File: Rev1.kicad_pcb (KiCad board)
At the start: 2 copper layers, 217.8 x 97.2 mm, 136 parts, among them J1 Screw_Terminal_01x02, J2 AVR-ISP-6, J3 UART Debug, J4 OLED I2C, Q1 MMBT2222ALT1G, Q10 NCE70T360D, Q11 NCE70T360D, Q2 NCE70T360D, Q3 NCE70T360D, Q4 NCE70T360D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

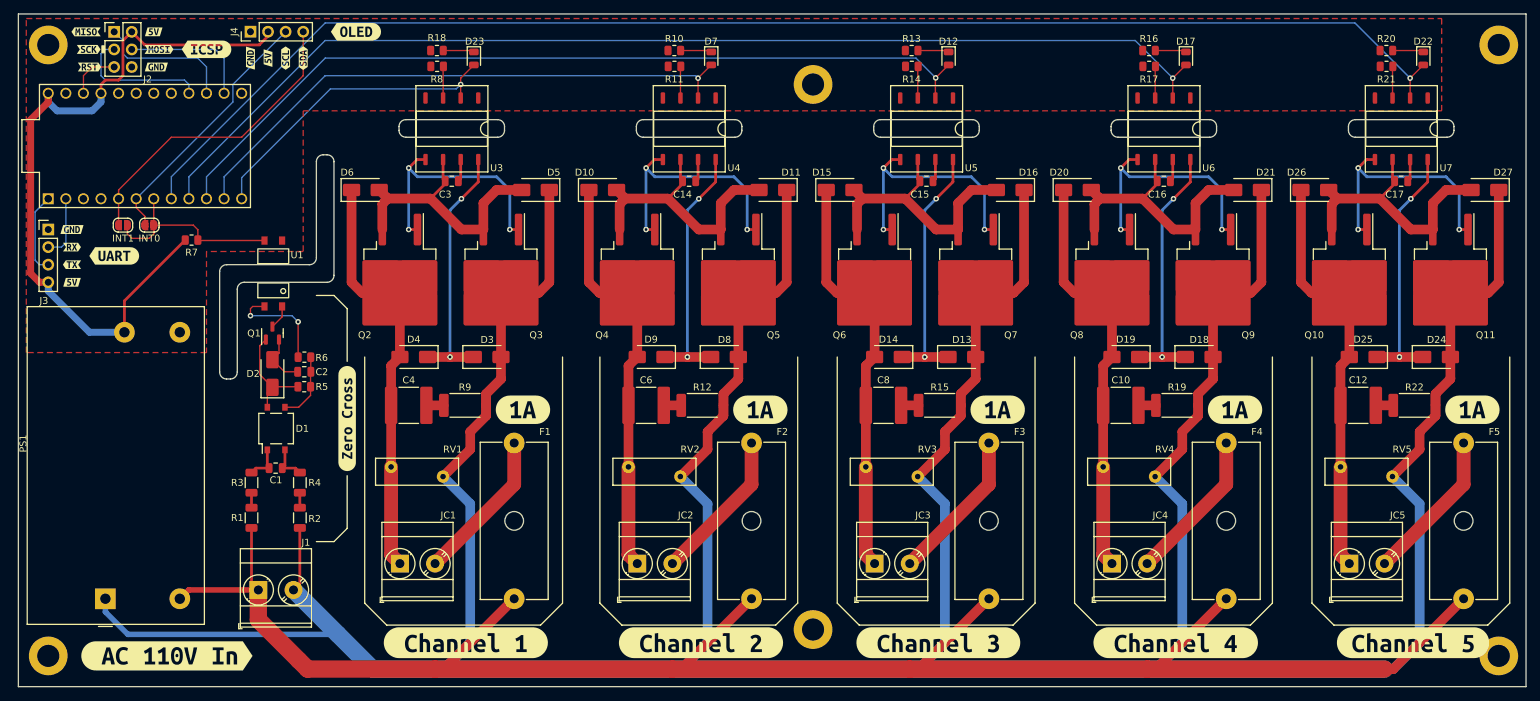
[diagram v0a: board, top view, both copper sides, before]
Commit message: Added changes based on Tim Williams feedback on StackExchange.
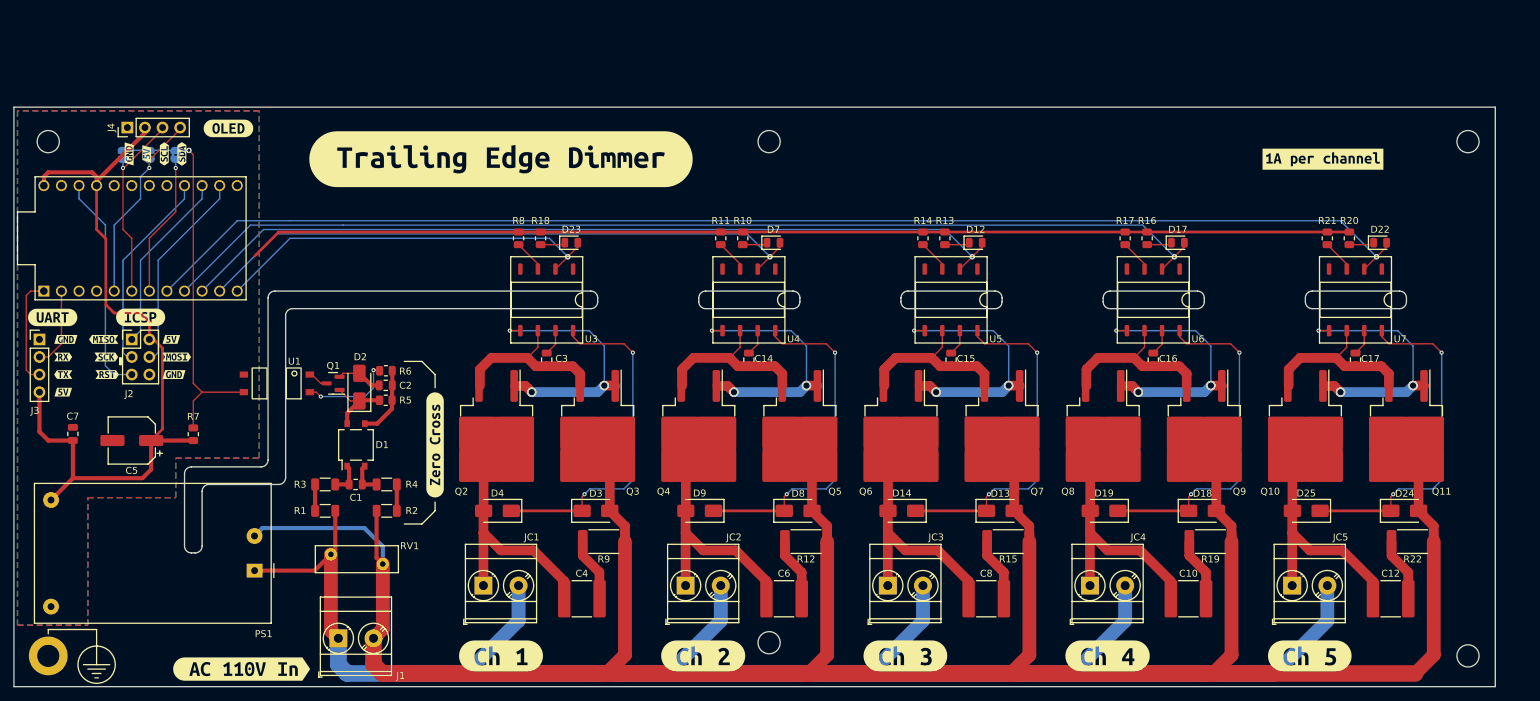
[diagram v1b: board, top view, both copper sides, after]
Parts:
- removed D10, D11, D15, D16, D20, D21, D26, D27, D5, D6: 1N4007, Diode_SMD:D_SMA
- removed F1, F2, F3, F4, F5: Fuse, Fuse:Fuseholder_Cylinder-5x20mm_Schurter_0031_8201_Horizontal_Open
- removed RV2, RV3, RV4, RV5: RM10D201KD1IE100, Varistor:RV_Disc_D12mm_W3.9mm_P7.5mm
- removed kibuzzard-6410FE0E: G***, kibuzzard-6410FE0E
- removed kibuzzard-6410FE18: G***, kibuzzard-6410FE18
- removed kibuzzard-6411021E: G***, kibuzzard-6411021E
- removed kibuzzard-64110278: G***, kibuzzard-64110278
- removed kibuzzard-6411027C: G***, kibuzzard-6411027C
- removed kibuzzard-64110283: G***, kibuzzard-64110283
- removed kibuzzard-6411028A: G***, kibuzzard-6411028A
- removed kibuzzard-6411049B: G***, kibuzzard-6411049B
- removed kibuzzard-64110629: G***, kibuzzard-64110629
- removed kibuzzard-64110646 (x5): G***, kibuzzard-64110646
- added C5: 47uF, Capacitor_SMD:CP_Elec_6.3x5.4, F.Cu at (55.2, 106.7)
- added C7: 100nF, Capacitor_SMD:C_0805_2012Metric, F.Cu at (46.7, 105.7)
- added JP3: ICP1, Jumper:SolderJumper-2_P1.3mm_Bridged2Bar_RoundedPad1.0x1.5mm, B.Cu at (61.6, 65.4)
- added kibuzzard-64132D73: G***, kibuzzard-64132D73, F.Cu at (43.8, 88.9)
- added kibuzzard-64132D7E: G***, kibuzzard-64132D7E, F.Cu at (56.5, 88.9)
- added kibuzzard-64132FD7: G***, kibuzzard-64132FD7, F.Cu at (69.2, 61.6)
- added kibuzzard-64133859: G***, kibuzzard-64133859, F.Cu at (71.1, 139.7)
- added kibuzzard-64136D9F: G***, kibuzzard-64136D9F, F.Cu at (108.6, 137.8)
- added kibuzzard-64136DB8: G***, kibuzzard-64136DB8, F.Cu at (137.8, 137.8)
- added kibuzzard-64136DD3: G***, kibuzzard-64136DD3, F.Cu at (167.0, 137.8)
- added kibuzzard-64136DE0: G***, kibuzzard-64136DE0, F.Cu at (196.2, 137.8)
- added kibuzzard-64136DEA: G***, kibuzzard-64136DEA, F.Cu at (225.4, 137.8)
- added kibuzzard-641373F0: G***, kibuzzard-641373F0, F.Cu at (108.6, 66.0)
- added kibuzzard-64137421: G***, kibuzzard-64137421, F.Cu at (227.3, 66.0)
- H1, H3, H4, H5, H6: footprint MountingHole:MountingHole_3.2mm_M3_DIN965_Pad -> MountingHole:MountingHole_3.2mm_M3_DIN965
- H2: value MountingHole -> MountingHole_Pad
- JP1, JP2: moved to B.Cu
- PS1: value IRM-05-5 -> HLK-PM01; footprint Converter_ACDC:Converter_ACDC_MeanWell_IRM-05-xx_THT -> Converter_ACDC:Converter_ACDC_HiLink_HLK-PMxx
- R10, R13, R16, R18, R20: value 180R -> 390R
- moved J2 44.5 mm to (55.2, 92.1)
- moved kibuzzard-6410DCCB 44.5 mm to (51.2, 92.1)
- moved kibuzzard-6410DCD5 44.5 mm to (61.0, 92.1)
- moved kibuzzard-6410DCF5 44.5 mm to (51.7, 97.2)
- moved kibuzzard-6410DD03 44.5 mm to (61.3, 97.2)
- moved kibuzzard-6410DCDD 44.5 mm to (51.6, 94.6)
- moved kibuzzard-6410DCE2 44.5 mm to (61.7, 94.6)
- moved C4 37.5 mm to (120.3, 129.5)
- moved C6 34.3 mm to (149.5, 129.5)
- moved C8 31.6 mm to (178.7, 129.5)
- moved R18 31.0 mm to (114.3, 77.5), turned to -90 degrees
- moved D23 30.1 mm to (118.7, 78.1), turned to 0 degrees
- moved C10 29.6 mm to (207.9, 129.5)
- moved C3 29.2 mm to (115.2, 95.0), turned to -90 degrees
- moved R10 28.9 mm to (143.5, 77.5), turned to -90 degrees
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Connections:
- H2 pad 1: (no net) -> Earth_Protective
- JC1 pad 2: Net-(JC1-Pin_2) -> /AC_L
- JC2 pad 2: Net-(JC2-Pin_2) -> /AC_L
- JC3 pad 2: Net-(JC3-Pin_2) -> /AC_L
- JC4 pad 2: Net-(JC4-Pin_2) -> /AC_L
- JC5 pad 2: Net-(JC5-Pin_2) -> /AC_L
- PS1 pad 1: /AC_N -> /AC_L
- PS1 pad 2: /AC_L -> /AC_N
- RV1 pad 1: /Sheetname: Dimmer Channel 1/LOAD -> /AC_L
- U2 pad 7: ZC -> Net-(JP3-B)
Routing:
- net /AC_N: track 619.7 -> 372.4 mm
- net GND: track 0.00 -> 159.5 mm
- net ZC: track 28.5 -> 57.0 mm, vias 0 -> 1
- net /RST: track 7.50 -> 31.9 mm
- net /Sheetname: Dimmer Channel 3/LOAD: track 61.1 -> 37.6 mm
- net /Sheetname: Dimmer Channel 2/LOAD: track 61.1 -> 37.6 mm
- net /Sheetname: Dimmer Channel 1/LOAD: track 61.1 -> 37.6 mm
- net /Sheetname: Dimmer Channel 4/LOAD: track 61.1 -> 37.6 mm
- net /Sheetname: Dimmer Channel 5/LOAD: track 61.1 -> 37.6 mm
- net Net-(JC5-Pin_2): track 22.2 -> 0.00 mm
- net Net-(JC4-Pin_2): track 22.2 -> 0.00 mm
- net Net-(JC3-Pin_2): track 22.2 -> 0.00 mm
- net Net-(JC2-Pin_2): track 22.2 -> 0.00 mm
- net Net-(JC1-Pin_2): track 22.2 -> 0.00 mm
- net Net-(JP3-B): track 0.00 -> 20.6 mm, vias 0 -> 1
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- added copper zone on B.Cu, net GND
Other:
- board size 217.8 x 97.2 mm -> 214 x 83.7 mm

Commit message: Added some test points. Added RS-485 Module. Updated PBC.
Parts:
- removed J4: OLED I2C, Connector_PinHeader_2.54mm:PinHeader_1x04_P2.54mm_Vertical
- removed the kibuzzard-6410DCD5 at (57.4, 65.3)
- removed the kibuzzard-6410DD03 at (54.9, 65.3)
- removed kibuzzard-6411054F: G***, kibuzzard-6411054F
- removed kibuzzard-64110558: G***, kibuzzard-64110558
- removed kibuzzard-64110884: G***, kibuzzard-64110884
- removed kibuzzard-64132FD7: G***, kibuzzard-64132FD7
- added H7: MountingHole, MountingHole:MountingHole_3.2mm_M3_DIN965, F.Cu at (81.3, 93.3)
- added TP1: TestPoint, TestPoint:TestPoint_THTPad_D2.0mm_Drill1.0mm, F.Cu at (115.6, 63.0)
- added TP10: TestPoint, TestPoint:TestPoint_THTPad_D2.0mm_Drill1.0mm, F.Cu at (179.8, 94.5)
- added TP11: TestPoint, TestPoint:TestPoint_THTPad_D2.0mm_Drill1.0mm, F.Cu at (209.0, 94.5)
- added TP12: TestPoint, TestPoint:TestPoint_THTPad_D2.0mm_Drill1.0mm, F.Cu at (238.3, 94.5)
- added TP13: TestPoint, TestPoint:TestPoint_THTPad_D2.0mm_Drill1.0mm, F.Cu at (125.5, 90.9)
- added TP14: TestPoint, TestPoint:TestPoint_THTPad_D2.0mm_Drill1.0mm, F.Cu at (154.7, 90.9)
- added TP15: TestPoint, TestPoint:TestPoint_THTPad_D2.0mm_Drill1.0mm, F.Cu at (183.9, 90.9)
- added TP16: TestPoint, TestPoint:TestPoint_THTPad_D2.0mm_Drill1.0mm, F.Cu at (213.1, 90.9)
- added TP17: TestPoint, TestPoint:TestPoint_THTPad_D2.0mm_Drill1.0mm, F.Cu at (242.3, 90.9)
- added TP2: TestPoint, TestPoint:TestPoint_THTPad_D2.0mm_Drill1.0mm, F.Cu at (144.8, 63.1)
- added TP3: TestPoint, TestPoint:TestPoint_THTPad_D2.0mm_Drill1.0mm, F.Cu at (173.7, 63.1)
- added TP4: TestPoint, TestPoint:TestPoint_THTPad_D2.0mm_Drill1.0mm, F.Cu at (203.2, 63.1)
- added TP5: TestPoint, TestPoint:TestPoint_THTPad_D2.0mm_Drill1.0mm, F.Cu at (232.2, 63.1)
- added TP6: TestPointZC, TestPoint:TestPoint_THTPad_D2.0mm_Drill1.0mm, F.Cu at (98.0, 63.0)
- added TP7: TestPointZC, TestPoint:TestPoint_THTPad_D2.0mm_Drill1.0mm, F.Cu at (88.4, 96.5)
- added TP8: TestPoint, TestPoint:TestPoint_THTPad_D2.0mm_Drill1.0mm, F.Cu at (121.4, 94.5)
- added TP9: TestPoint, TestPoint:TestPoint_THTPad_D2.0mm_Drill1.0mm, F.Cu at (150.6, 94.5)
- added U8: RS485_MODULE, 0x3333:RS485_MODULE, F.Cu at (46.4, 81.3)
- JP1, JP2, JP3: moved to F.Cu
- moved kibuzzard-64137421 71.4 mm to (156.0, 68.6)
- moved kibuzzard-6410D85E 51.4 mm to (81.3, 62.9)
- moved kibuzzard-6410D834 47.7 mm to (80.9, 65.4)
- moved kibuzzard-6410D800 44.7 mm to (81.3, 68.0)
- moved H1 44.5 mm to (87.6, 62.9)
- moved R7 41.9 mm to (95.9, 78.5), turned to 90 degrees
- moved J3 41.6 mm to (77.5, 70.5), turned to 180 degrees
- moved kibuzzard-6410D86B 41.6 mm to (81.3, 70.5)
- moved kibuzzard-64132D73 38.4 mm to (79.4, 74.3)
- moved U1 24.3 mm to (97.3, 86.4), turned to 90 degrees
- moved JP2 13.9 mm to (63.5, 75.6), turned to 180 degrees
- moved Q1 13.3 mm to (97.3, 95.2), turned to 90 degrees
- moved JP3 12.8 mm to (63.5, 78.1), turned to 180 degrees
- moved D2 12.5 mm to (97.8, 106.9)
- moved C5 11.1 mm to (44.2, 107.7)
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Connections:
- net /RX renamed RX
- net /TX renamed TX
- U2 pad 17: unconnected-(U2-PF7/D18/ADC7-Pad17) -> ME
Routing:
- net GND: track 159.5 -> 0.00 mm
- net +5V: track 108.5 -> 169.3 mm
- net RX: track 11.6 -> 70.3 mm
- net TX: track 15.8 -> 66.3 mm, vias 0 -> 2
- net ME: track 0.00 -> 40.9 mm
- net TRG_1: track 57.2 -> 88.8 mm
- net TRG_2: track 89.4 -> 117.4 mm
- net /RST: track 31.9 -> 59.4 mm
- net TRG_3: track 121.7 -> 147.8 mm
- net TRG_4: track 154.0 -> 177.9 mm
- net TRG_5: track 186.3 -> 208.3 mm
- net SDA: track 28.9 -> 6.97 mm, vias 1 -> 0
- net SCL: track 27.9 -> 6.97 mm, vias 1 -> 0
- net Net-(JP3-B): track 20.6 -> 6.97 mm, vias 1 -> 0
- net Net-(D1--): track 10.5 -> 22.7 mm
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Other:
- outline, holes or cut-outs redrawn

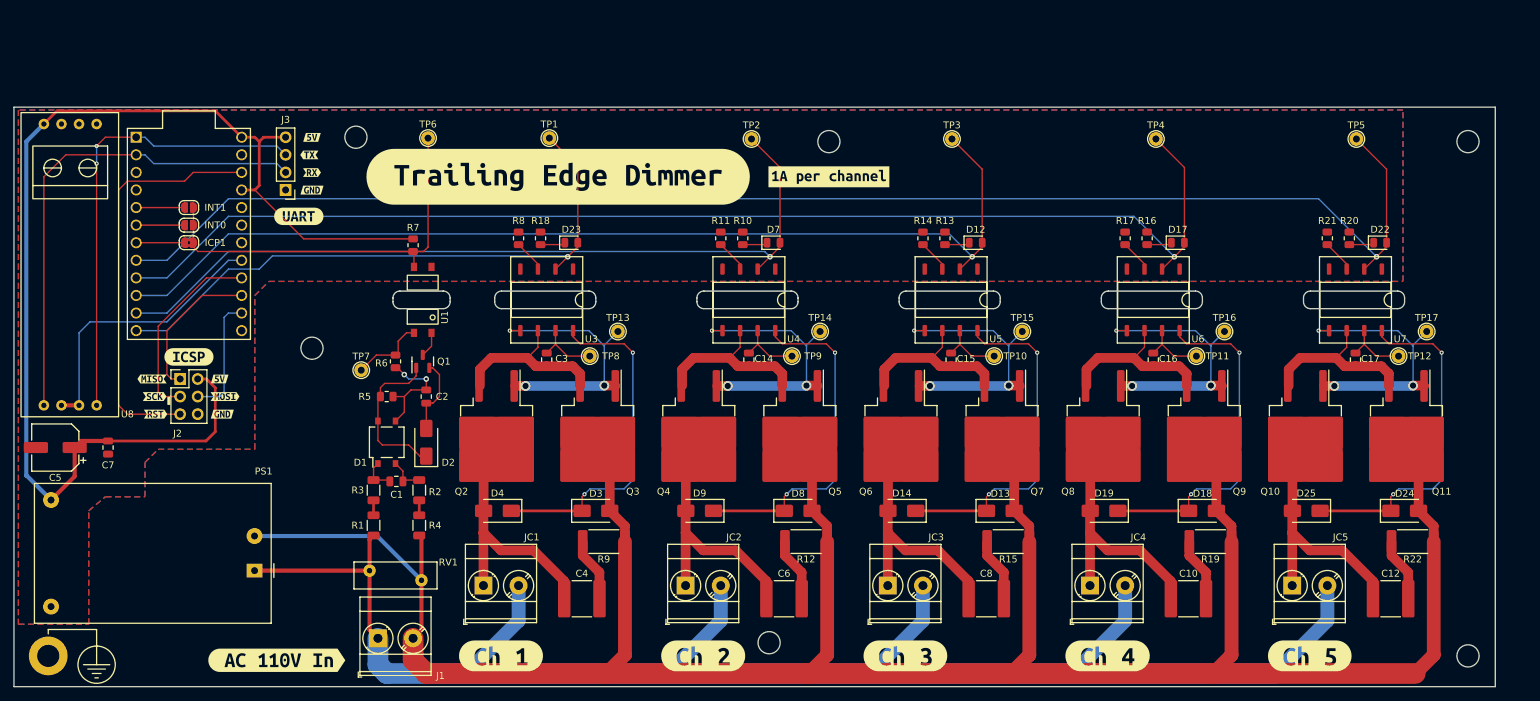
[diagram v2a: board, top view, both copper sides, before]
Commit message: Added stitching vias.
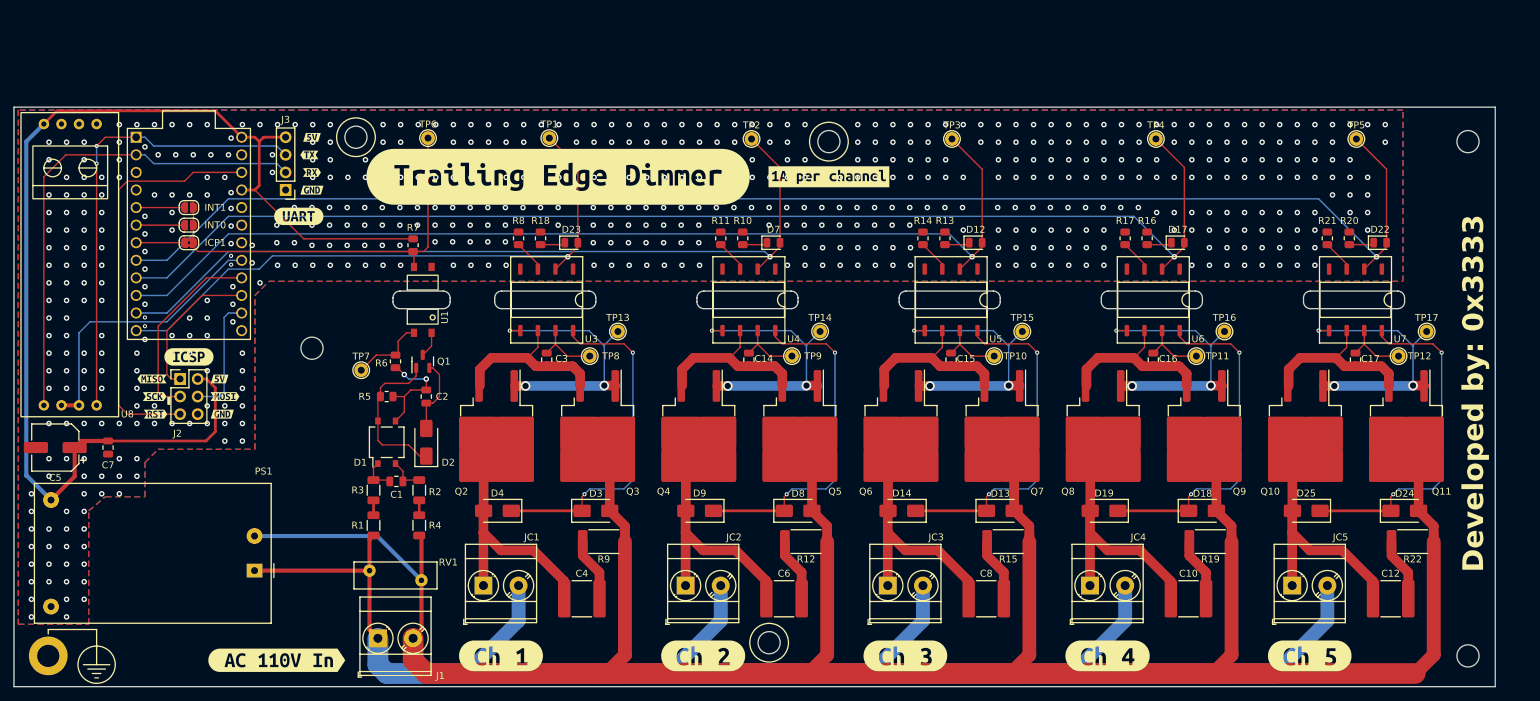
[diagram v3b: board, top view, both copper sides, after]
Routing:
- net GND: vias 0 -> 586
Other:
- board text added: "Developed by: 0x3333"
